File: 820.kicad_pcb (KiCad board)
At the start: 4 copper layers, 48 x 105 mm, 124 parts, among them J1 PJ301BM, J10 PJ301BM, J2 PJ301BM, J4 PJ301BM, J5 PJ301BM, J6 PJ301BM, J7 PJ301BM, J8 PJ301BM, J9 PJ301BM, P1 CONN_02X05, P2 CONN_01X03, P3 CONN_01X08, Q1 2SC4207, Q2 PMBT2369, Q3 MMBF4391LT1G, Q4 2SA1832, Q5 PMBT2369, SW1 SPDT, U1 OPA2180, U2 TL072-, U3 TL072-, U4 TL072-, U5 TA75S558F

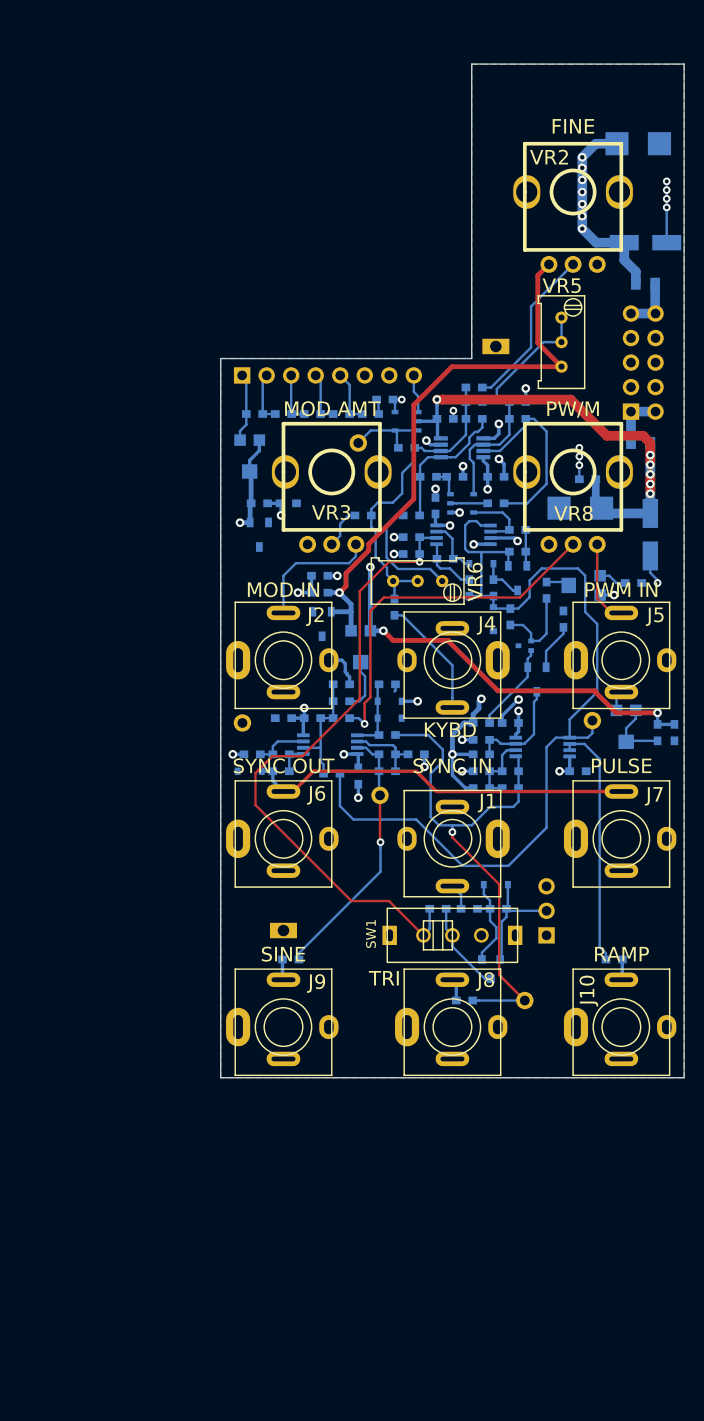
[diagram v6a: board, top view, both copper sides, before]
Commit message: changed 2SC4207 NPN pair to BCM847 matched pair.
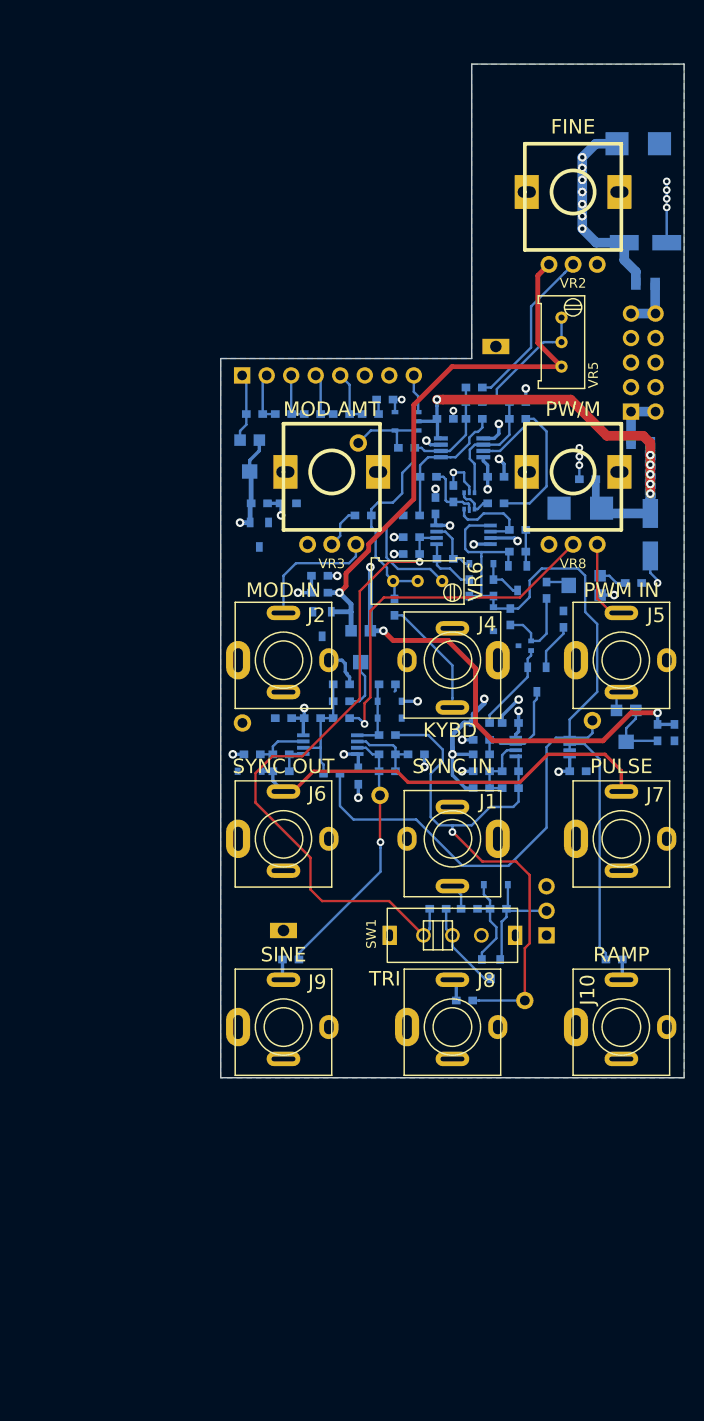
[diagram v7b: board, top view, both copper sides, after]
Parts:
- Q1: value 2SC4207 -> BCM847; footprint MyModules:SOT753_TSOP5_SC-74A -> TO_SOT_Packages_SMD:SOT-666
- R18: value 1.5M -> 1meg
- R43: value 8.2K -> 7.5K
- R47: value 10K -> 12K
- R48: value 15K -> 10K
- VR2, VR3, VR8: footprint MyModules:RD901F-ALPHA-POT-T18 -> MyModules:RD901F-40-ALPHA-POT-T18
- moved TC1 1.76 mm to (116.1, 82.5), turned to 90 degrees
- moved Q1 0.79 mm to (117.8, 83.2), turned to 270 degrees
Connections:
- Q1 pad 1: GND -> Net-(Q1-Pad1)
- Q1 pad 2: Net-(Q1-Pad2) -> GND
- Q1 pad 3: Net-(Q1-Pad3) -> Net-(C15-Pad1)
- Q1 pad 4: Net-(C15-Pad1) -> Net-(Q1-Pad1)
- R17 pad 2: Net-(Q1-Pad3) -> Net-(Q1-Pad5)
- R19 pad 2: Net-(Q1-Pad2) -> Net-(Q1-Pad1)
- R21 pad 1: Net-(Q1-Pad5) -> Net-(Q1-Pad6)
- TC1 pad 1: Net-(Q1-Pad3) -> Net-(Q1-Pad5)
- U2 pad 2: Net-(Q1-Pad5) -> Net-(Q1-Pad6)
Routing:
- net Net-(Q1-Pad6): track 0.00 -> 9.28 mm
- net Net-(Q1-Pad1): track 0.00 -> 3.99 mm
- net Net-(Q1-Pad2): track 3.85 -> 0.00 mm
- net /PULSE: track 49.9 -> 53.6 mm
- net Net-(Q1-Pad3): track 3.01 -> 0.00 mm
- net GND: track 45.5 -> 48.1 mm, vias 25 -> 24
- net Net-(C19-Pad2): track 55.0 -> 57.5 mm
- net SYNC: track 66.3 -> 68.0 mm
- net +10V: track 121.7 -> 123.1 mm
- net Net-(Q1-Pad5): track 7.21 -> 6.44 mm
- net Net-(C17-Pad2): track 94.8 -> 94.2 mm
- added copper zone on B.Cu, net -12V

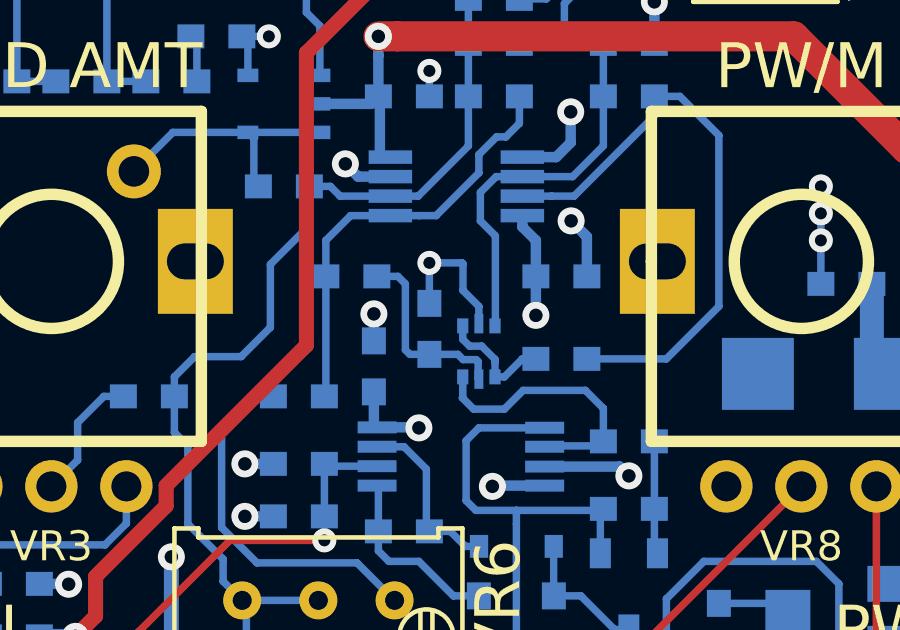
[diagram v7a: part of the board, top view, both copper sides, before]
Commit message: PMP4201 NPN matched pair replaces BCM847
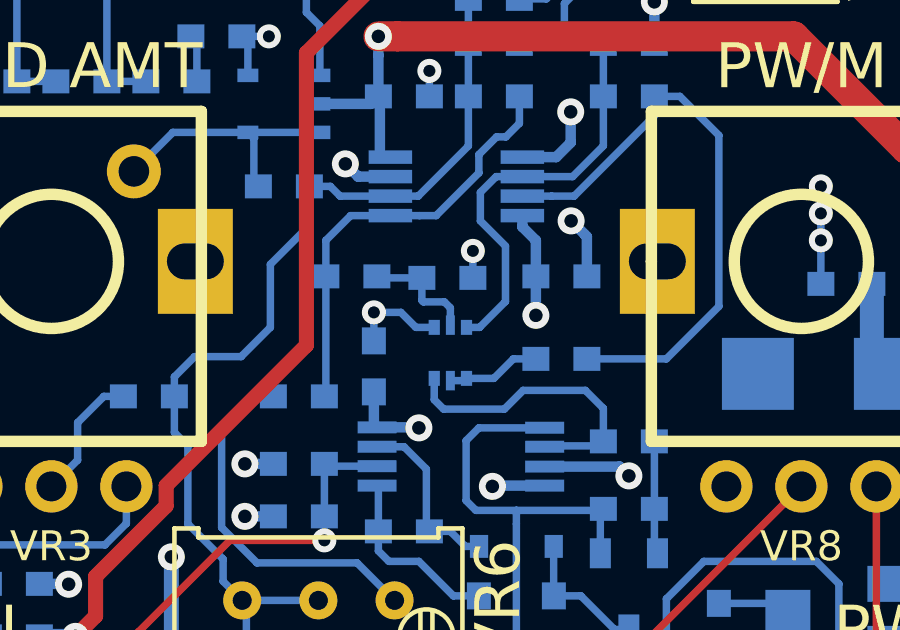
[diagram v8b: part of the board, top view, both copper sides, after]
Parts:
- Q1: value BCM847 -> PMP4201
- moved TC1 1.80 mm to (116.7, 80.8), turned to 0 degrees
- moved Q1 0.95 mm to (116.8, 83.3)
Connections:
- Q1 pad 1: Net-(Q1-Pad1) -> GND
- Q1 pad 2: GND -> Net-(Q1-Pad2)
- Q1 pad 4: Net-(Q1-Pad1) -> Net-(Q1-Pad4)
- Q1 pad 5: Net-(Q1-Pad5) -> Net-(Q1-Pad4)
- R17 pad 2: Net-(Q1-Pad5) -> Net-(Q1-Pad2)
- R19 pad 2: Net-(Q1-Pad1) -> Net-(Q1-Pad4)
- TC1 pad 1: Net-(Q1-Pad5) -> Net-(Q1-Pad2)
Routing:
- net Net-(Q1-Pad5): track 6.44 -> 0.00 mm
- net Net-(Q1-Pad1): track 3.99 -> 0.00 mm
- net Net-(Q1-Pad2): track 0.00 -> 3.90 mm
- net Net-(Q1-Pad4): track 0.00 -> 3.15 mm
- net GND: track 48.1 -> 46.6 mm
- net Net-(C15-Pad1): track 12.8 -> 13.8 mm
- net Net-(Q1-Pad6): track 9.28 -> 10.2 mm
